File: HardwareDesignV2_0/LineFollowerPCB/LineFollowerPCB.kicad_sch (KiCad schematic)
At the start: 11 parts, among them J1 B2B-XH-A, J2 B4B-XH-A, J3 Conn_01x04, M1 Motor_DC, M2 Motor_DC, U1 Black Pill v2, U2 DRV8833, U3 AMS1117-3.3, U4 SX1308

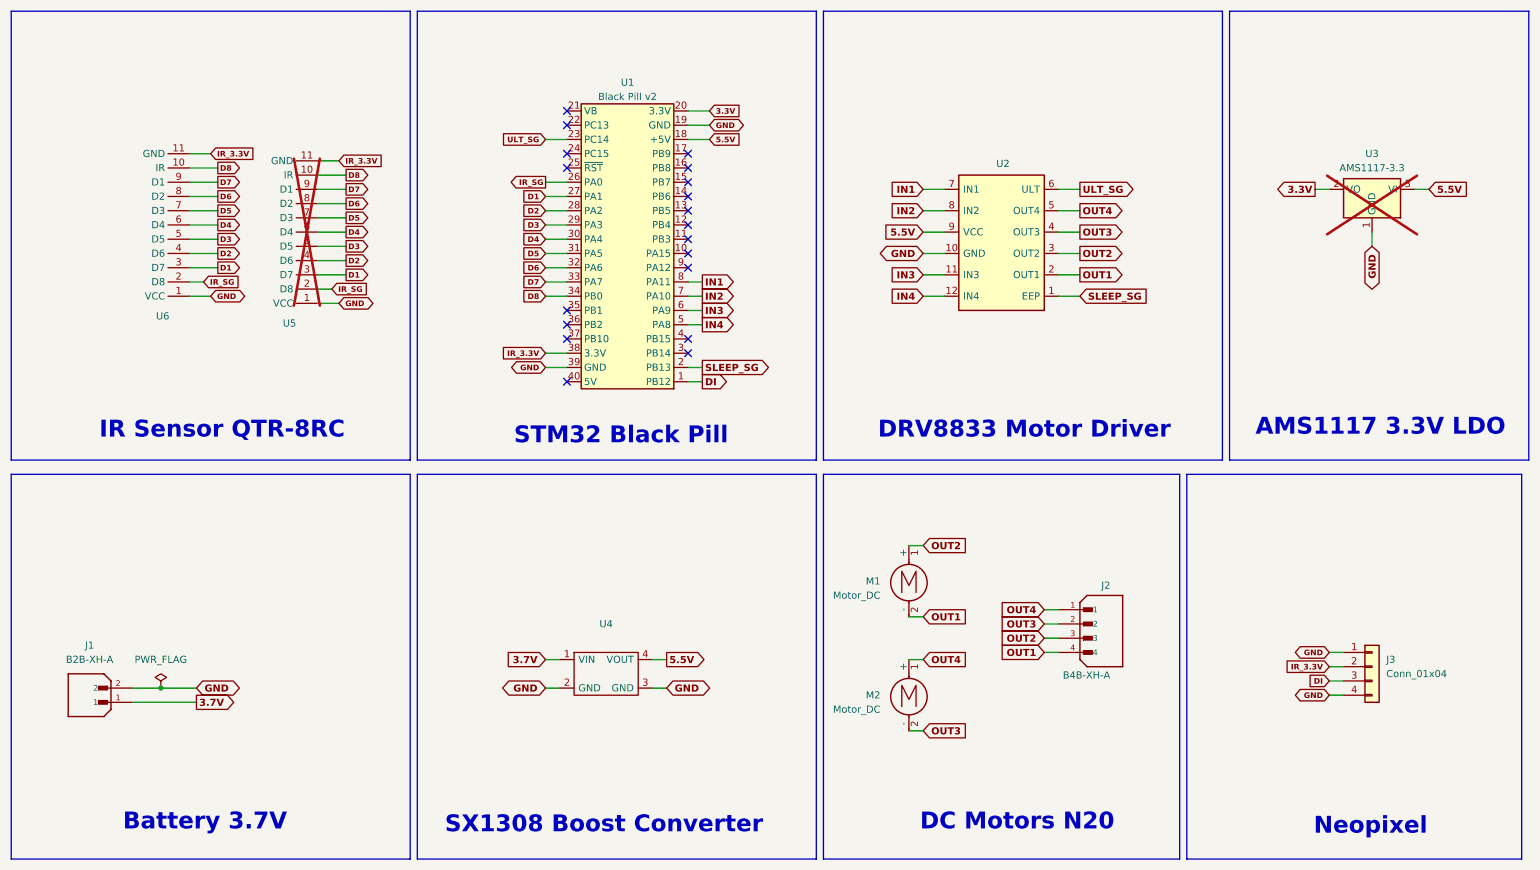
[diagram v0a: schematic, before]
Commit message: - Update the schematic design - Fix the pins arrangment of the cytron sensor - Create the Cytron sensor footprint - Add the Cytron sensor 3D model - Add the 1N4001 doide - Update the layout
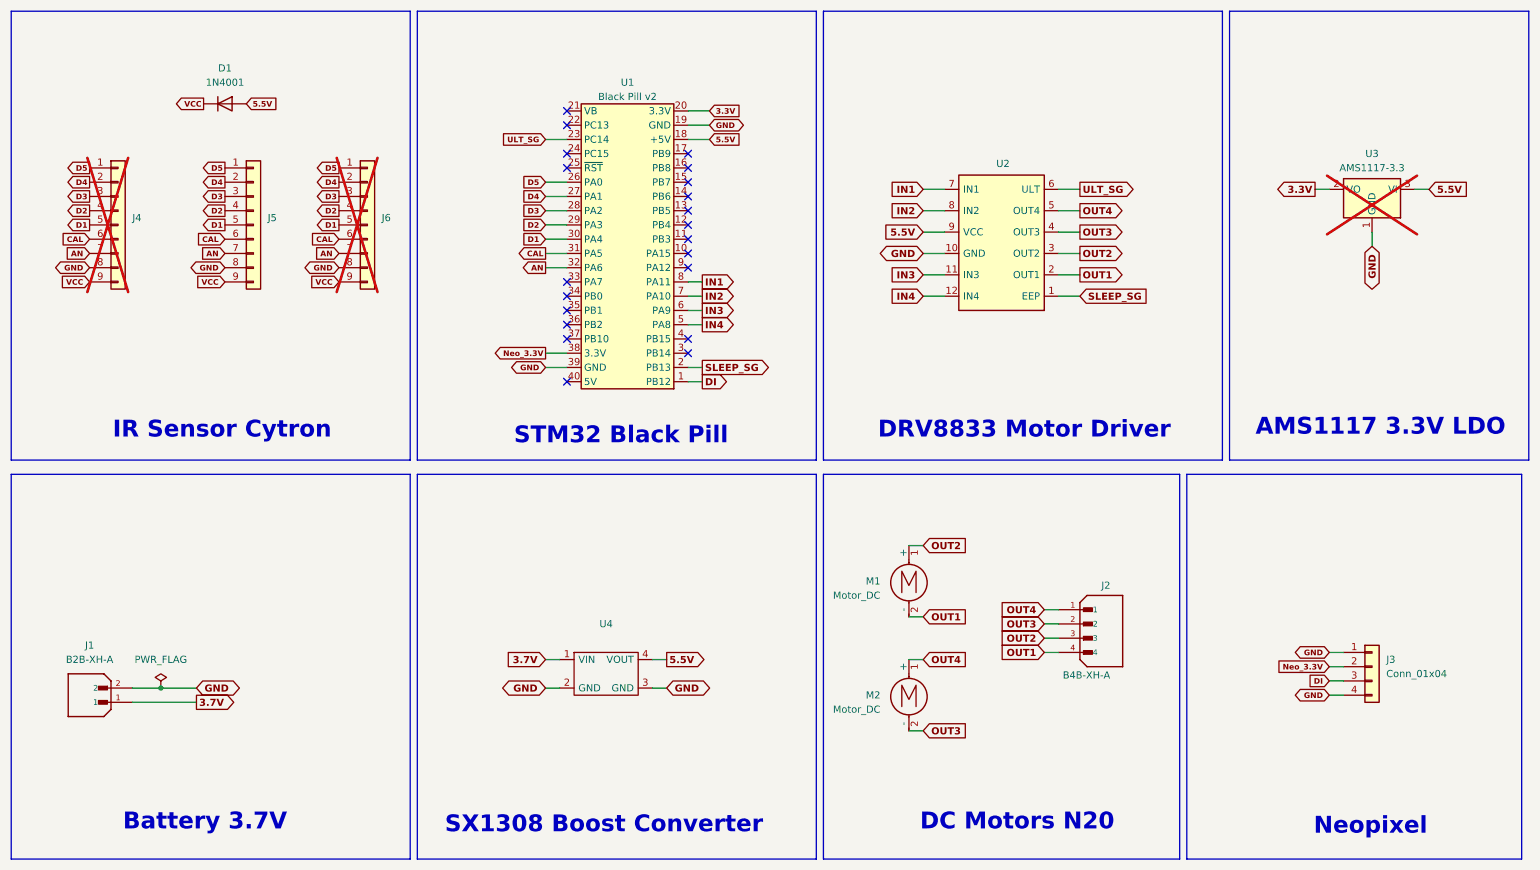
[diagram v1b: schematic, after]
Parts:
- removed U5, U6: ~, Connector_PinHeader_2.54mm:PinHeader_1x11_P2.54mm_Vertical, symbol Connector:QTR-8RC
- added D1: 1N4001, Diode_THT:D_DO-41_SOD81_P10.16mm_Horizontal, symbol Diode:1N4001
- added J4, J5, J6: Conn_01x09, CytronLineMaker:CytronIR_Sensor, symbol Connector_Generic:Conn_01x09
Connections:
- net IR_SG is gone; now on net D5: U1.26 (PA0)
- net 5.5V: now also D1.2 (A)
- net D1: now also U1.30 (PA4), J4.5 (Pin_5), J5.5 (Pin_5), J6.5 (Pin_5); no longer U1.27 (PA1)
- net D2: now also U1.29 (PA3), J4.4 (Pin_4), J5.4 (Pin_4), J6.4 (Pin_4); no longer U1.28 (PA2)
- net D3: now also U1.28 (PA2), J4.3 (Pin_3), J5.3 (Pin_3), J6.3 (Pin_3); no longer U1.29 (PA3)
- net D4: now also U1.27 (PA1), J4.2 (Pin_2), J5.2 (Pin_2), J6.2 (Pin_2); no longer U1.30 (PA4)
- net D5: now also J4.1 (Pin_1), J5.1 (Pin_1), J6.1 (Pin_1); no longer U1.31 (PA5)
- net GND: now also J4.8 (Pin_8), J5.8 (Pin_8), J6.8 (Pin_8)
- net D6 renamed AN
- net AN: now also J4.7 (Pin_7), J5.7 (Pin_7), J6.7 (Pin_7)
- net D7: no longer names the net of U1.33 (PA7)
- net D8: no longer names the net of U1.34 (PB0)
- net IR_3.3V renamed Neo_3.3V
- new net CAL: J4.6 (Pin_6), J5.6 (Pin_6), J6.6 (Pin_6), U1.31 (PA5)
- new net VCC: D1.1 (K), J4.9 (Pin_9), J5.9 (Pin_9), J6.9 (Pin_9)
- no-connect marks 19 -> 21
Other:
- note added: "IR Sensor Cytron"
- note removed: "IR Sensor QTR-8RC"
